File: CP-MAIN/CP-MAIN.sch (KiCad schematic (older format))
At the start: 32 parts, among them J1 power, J2 Serial, J3 USB_A, J4 w-Sensor1, J5 i2c, J6 w-Sensor2, J7 w-Sensor3, Q1 Q_NMOS_GSD, Q2 Q_NMOS_GSD, Q3 Q_NMOS_GSD, U1 R-783.3-0.5, U2 AE-ATMEGA328-MINI, U3 TWELITE_DIP

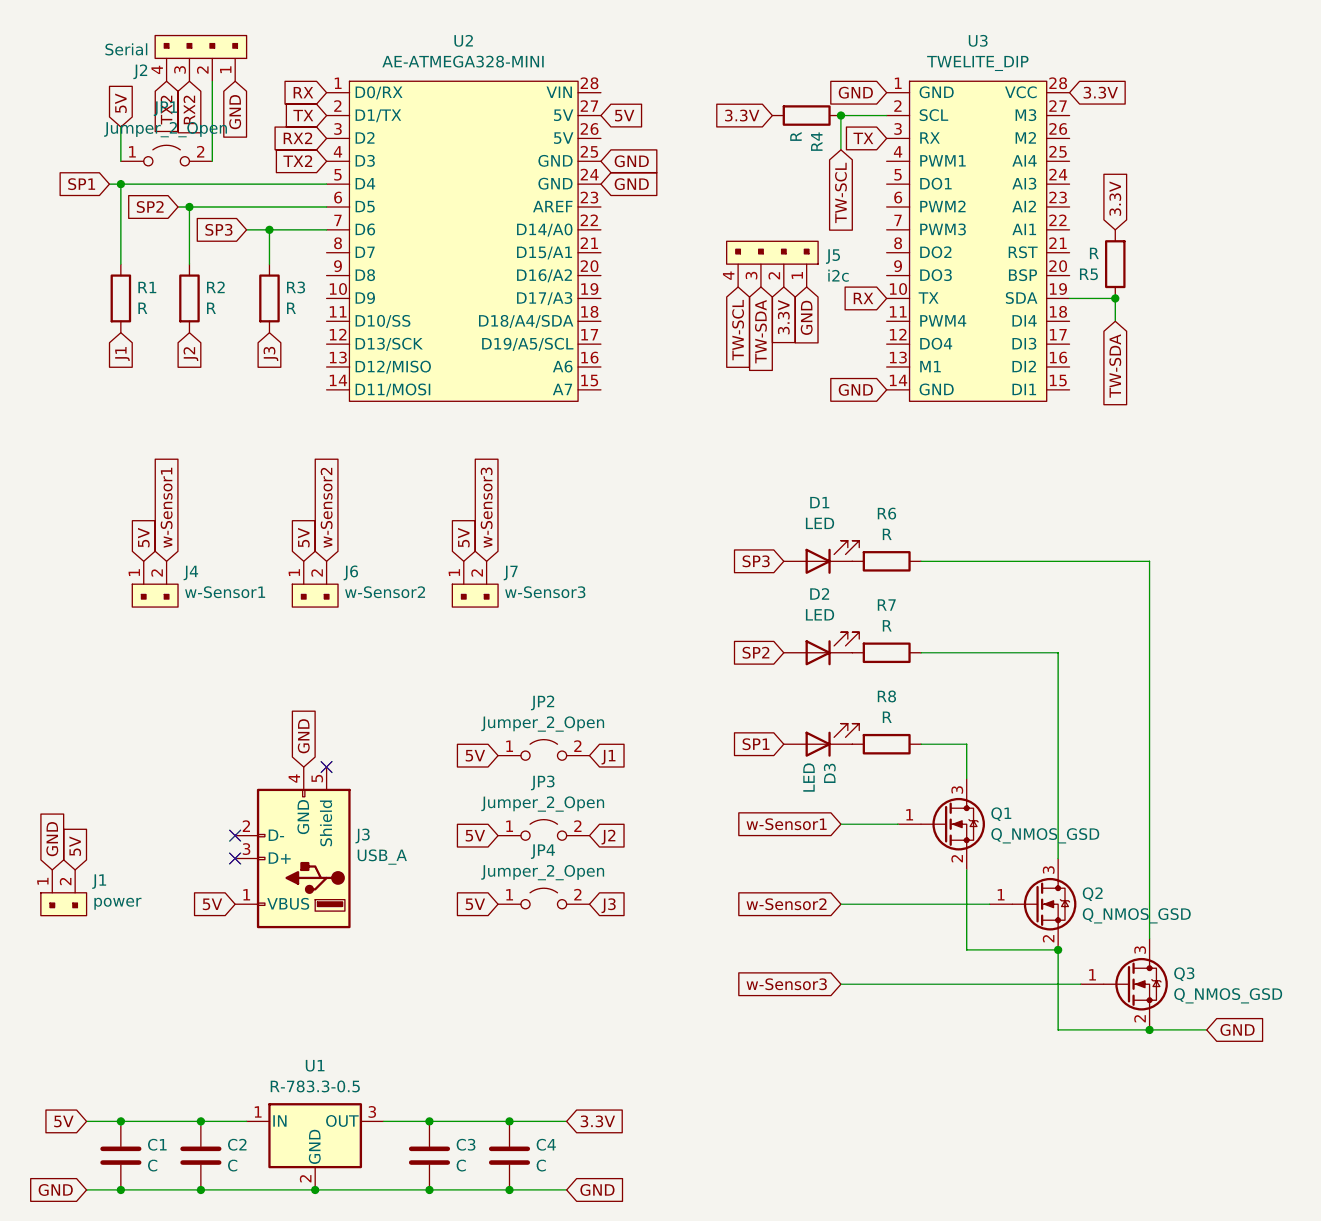
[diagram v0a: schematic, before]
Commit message: ・CP-MAIN水位センサアナログ入力用に変更
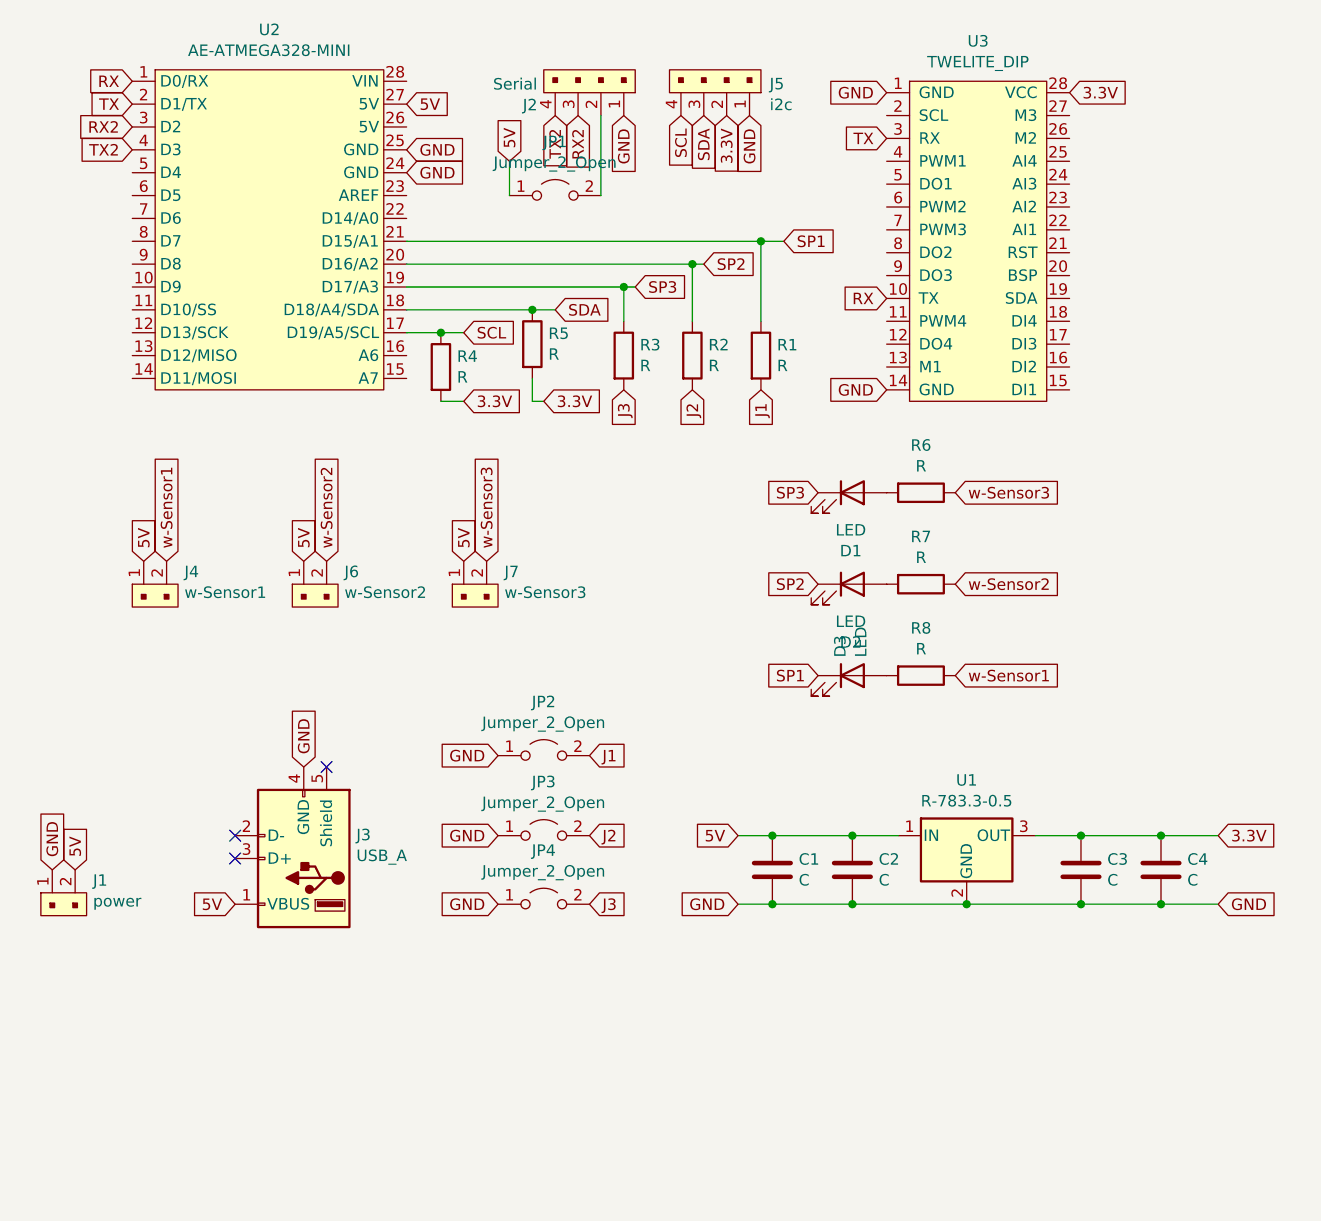
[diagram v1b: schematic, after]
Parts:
- removed Q1, Q2, Q3: Q_NMOS_GSD, digikey-footprints:SOT-23W, symbol Device:Q_NMOS_GSD
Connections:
- net 5V: no longer JP2.1 (A), JP3.1 (A), JP4.1 (A)
- net GND: now also JP2.1 (A), JP3.1 (A), JP4.1 (A)
- net SP1: now also D3.1 (K), U2.21 (D15/A1); no longer D3.2 (A), U2.5 (D4)
- net SP2: now also D2.1 (K), U2.20 (D16/A2); no longer D2.2 (A), U2.6 (D5)
- net SP3: now also D1.1 (K), U2.19 (D17/A3); no longer D1.2 (A), U2.7 (D6)
- net w-Sensor1: now also R8.1
- net w-Sensor2: now also R7.1
- net w-Sensor3: now also R6.1
- net SCL: now reaches U2.17 (D19/A5/SCL)
- net SCL: now also J5.4, R4.1
- net SDA: now reaches U2.18 (D18/A4/SDA)
- net SDA: now also J5.3, R5.1
- net at R8.2: now also D3.2 (A); no longer D3.1 (K)
- net at R7.2: now also D2.2 (A); no longer D2.1 (K)
- net at R6.2: now also D1.2 (A); no longer D1.1 (K)
- removed net TW-SCL: J5.4, R4.1, U3.2 (SCL)
- removed net TW-SDA: J5.3, R5.1, U3.19 (SDA)
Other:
- moved on the sheet: C1, C2, C3, C4, D1, D2, D3, J2, J5, JP1, R1, R2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
